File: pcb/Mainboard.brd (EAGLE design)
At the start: 28 x 55 mm, 13 parts

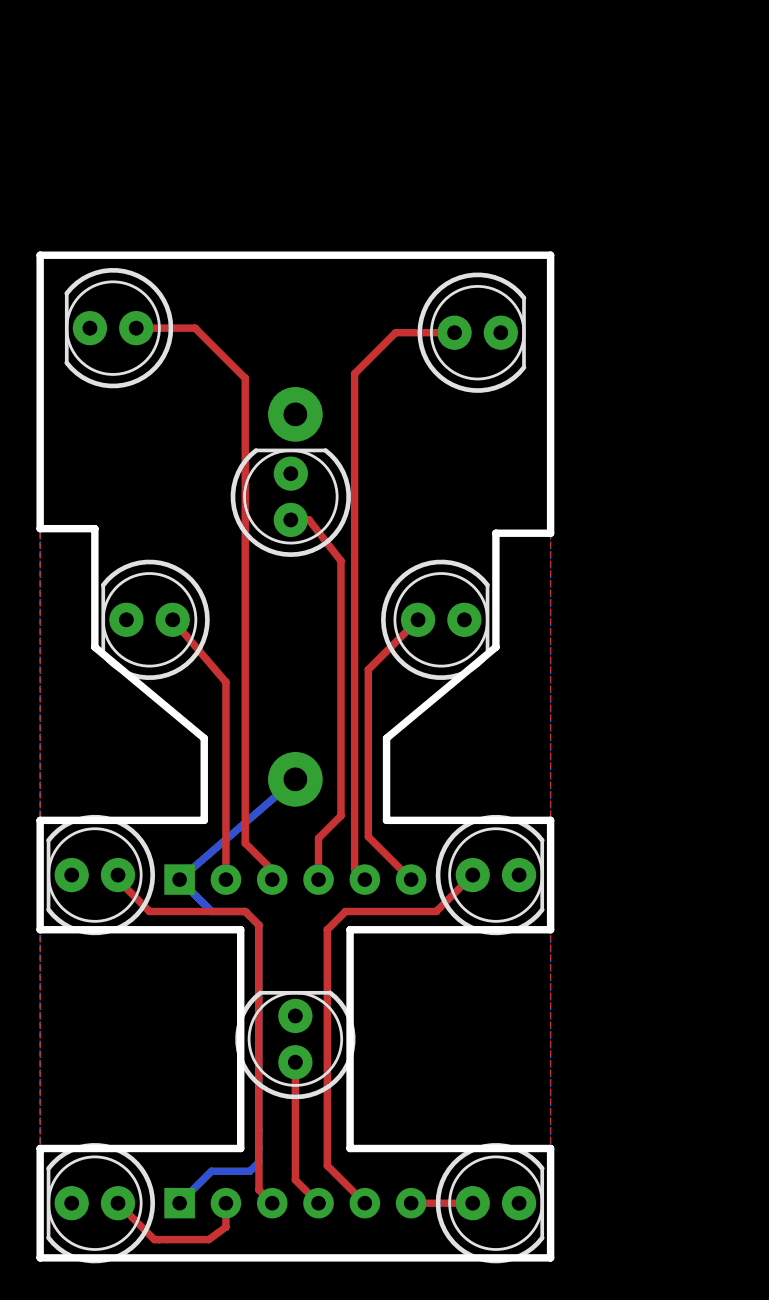
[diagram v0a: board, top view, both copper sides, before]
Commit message: Started SMD redesign.
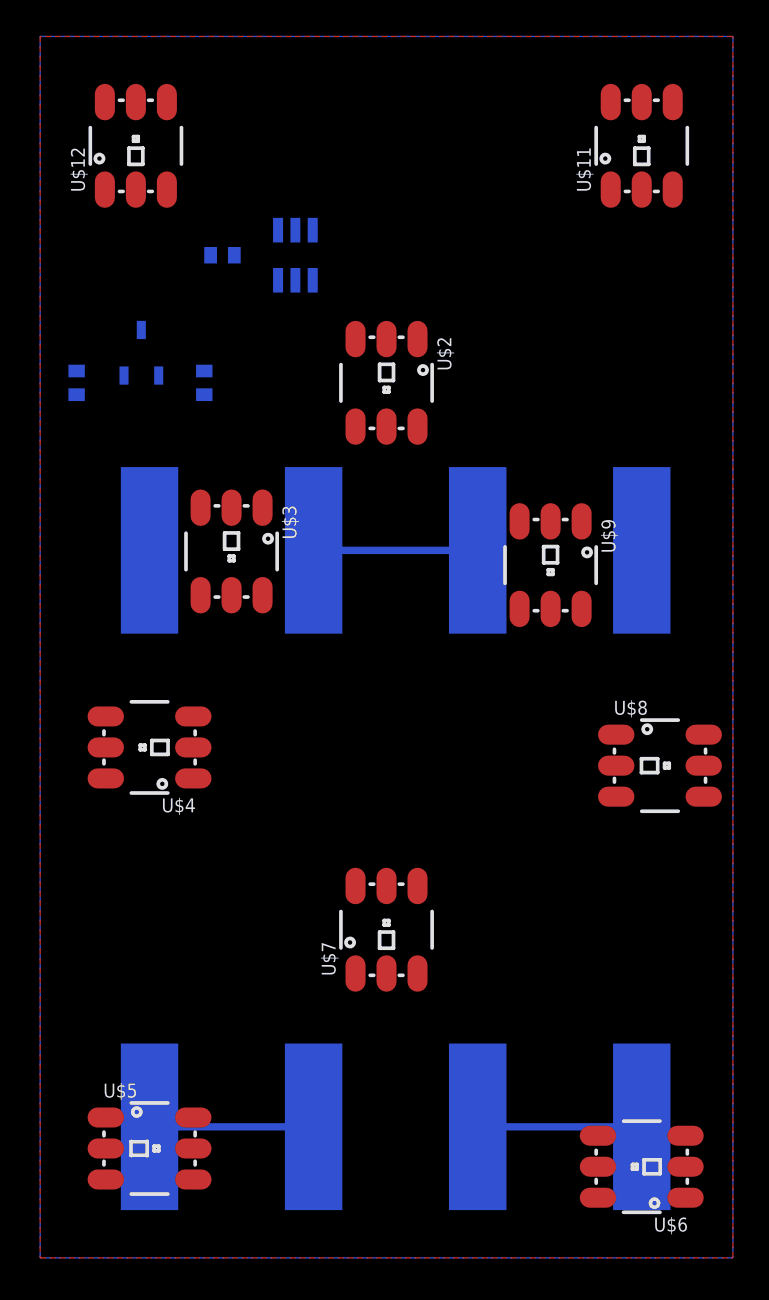
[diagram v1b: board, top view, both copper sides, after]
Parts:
- removed D1, D10, D2, D3, D4, D5, D6, D7, D8, D9: (no value), SparkFun-LED:LED5MM
- removed R1, R2: 150, SparkFun-Resistors:RPACK-SIP-PTH-5
- added C1: 0.1uF, SparkFun-Passives:0402-CAP
- added C2, C3: 1uF, SparkFun-Passives:0402-CAP
- added FRAME1: FRAME-LETTER, SparkFun-Aesthetics:CREATIVE_COMMONS
- added U$11, U$12, U$2, U$3, U$4, U$5, U$6, U$7, U$8, U$9: APA102C, OpenSourceArt_Eagle_Library:LED-TRICOLOR-5050-IC
- added U$13, U$14, U$15, U$16: (no value), OpenSourceArt_Eagle_Library:KEYSTONE-SMD-AAAA-CLIPS
- added U$17: MCP1700, OpenSourceArt_Eagle_Library:MCP1700
- U$1: value KEYSTONE-TH-CR2450 -> ATTINY4/5/9/10; device winn:KEYSTONE-TH-CR2450 -> OpenSourceArt_Eagle_Library:SOT23-6
- moved U$1 14.0 mm to (14.0, 55.0), turned to 180 degrees
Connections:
- removed net N$7: D6.A, R2.P$2
- removed net VCC: R1.P$1, R2.P$1, U$1.POS
- new net 3.3V: C1.1, C3.1, U$1.5, U$11.4, U$12.4, U$17.VOUT, U$2.4, U$3.4, U$4.4, U$5.4, U$6.4, U$7.4, U$8.4, U$9.4
- new net MOSI: U$1.1, U$2.1
- new net N$11: U$4.6, U$5.1
- new net N$12: U$3.6, U$4.1
- new net N$13: U$7.6, U$8.1
- new net N$14: U$7.5, U$8.2
- new net N$15: U$8.6, U$9.1
- new net N$16: U$8.5, U$9.2
- new net N$17: U$11.1, U$9.6
- new net N$18: U$11.2, U$9.5
- new net N$19: U$11.6, U$12.1
- new net N$20: U$11.5, U$12.2
- new net N$23: U$14.P$2, U$15.P$1
- new net N$24: U$15.P$2, U$16.P$1
- new net SCK: U$1.3, U$2.2
- new net V_BATT: C2.1, U$13.P$1, U$17.VIN
- net GND: now also C1.2, C2.2, C3.2, U$1.2, U$11.3, U$12.3, U$16.P$2, U$17.GND, U$2.3, U$3.3, U$4.3, U$5.3, U$6.3, U$7.3, U$8.3, U$9.3; no longer D1.K, D10.K, D2.K, D3.K, D4.K, D5.K, D6.K, D7.K, D8.K, D9.K, U$1.NEG
- net N$1: now also U$2.6, U$3.1; no longer D4.A, R1.P$5
- net N$10: now also U$5.6, U$6.1; no longer D10.A, R2.P$6
- net N$2: now also U$2.5, U$3.2; no longer D1.A, R1.P$2
- net N$3: now also U$3.5, U$4.2; no longer D2.A, R1.P$3
- net N$4: now also U$4.5, U$5.2; no longer D3.A, R1.P$4
- net N$5: now also U$5.5, U$6.2; no longer D5.A, R1.P$6
- net N$6: now also U$13.P$2, U$14.P$1; no longer D7.A, R2.P$3
- net N$8: now also U$6.5, U$7.2; no longer D9.A, R2.P$5
- net N$9: now also U$6.6, U$7.1; no longer D8.A, R2.P$4
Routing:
- net N$3: track 35.2 -> 0.00 mm
- net N$1: track 34.5 -> 0.00 mm
- net VCC: track 32.1 -> 0.00 mm
- net N$8: track 25.1 -> 0.00 mm
- net N$4: track 21.8 -> 0.00 mm
- net N$5: track 16.4 -> 0.00 mm
- net N$6: track 24.6 -> 9.00 mm
- net N$2: track 15.3 -> 0.00 mm
- net N$24: track 0.00 -> 9.00 mm
- net N$23: track 0.00 -> 9.00 mm
- net N$7: track 8.28 -> 0.00 mm
- net N$9: track 8.26 -> 0.00 mm
- net N$10: track 3.38 -> 0.00 mm
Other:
- board outline removed
